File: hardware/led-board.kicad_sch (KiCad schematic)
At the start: 65 parts, among them J1 XT60PW-M, J2 PROG, J3 I2C, J4 CAN2, J5 XT30PW-F, J6 XT30PW-F, J7 MR30PW-FB, Q1 NCE0115K, Q2 NCE0115K, Q3 BSS138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

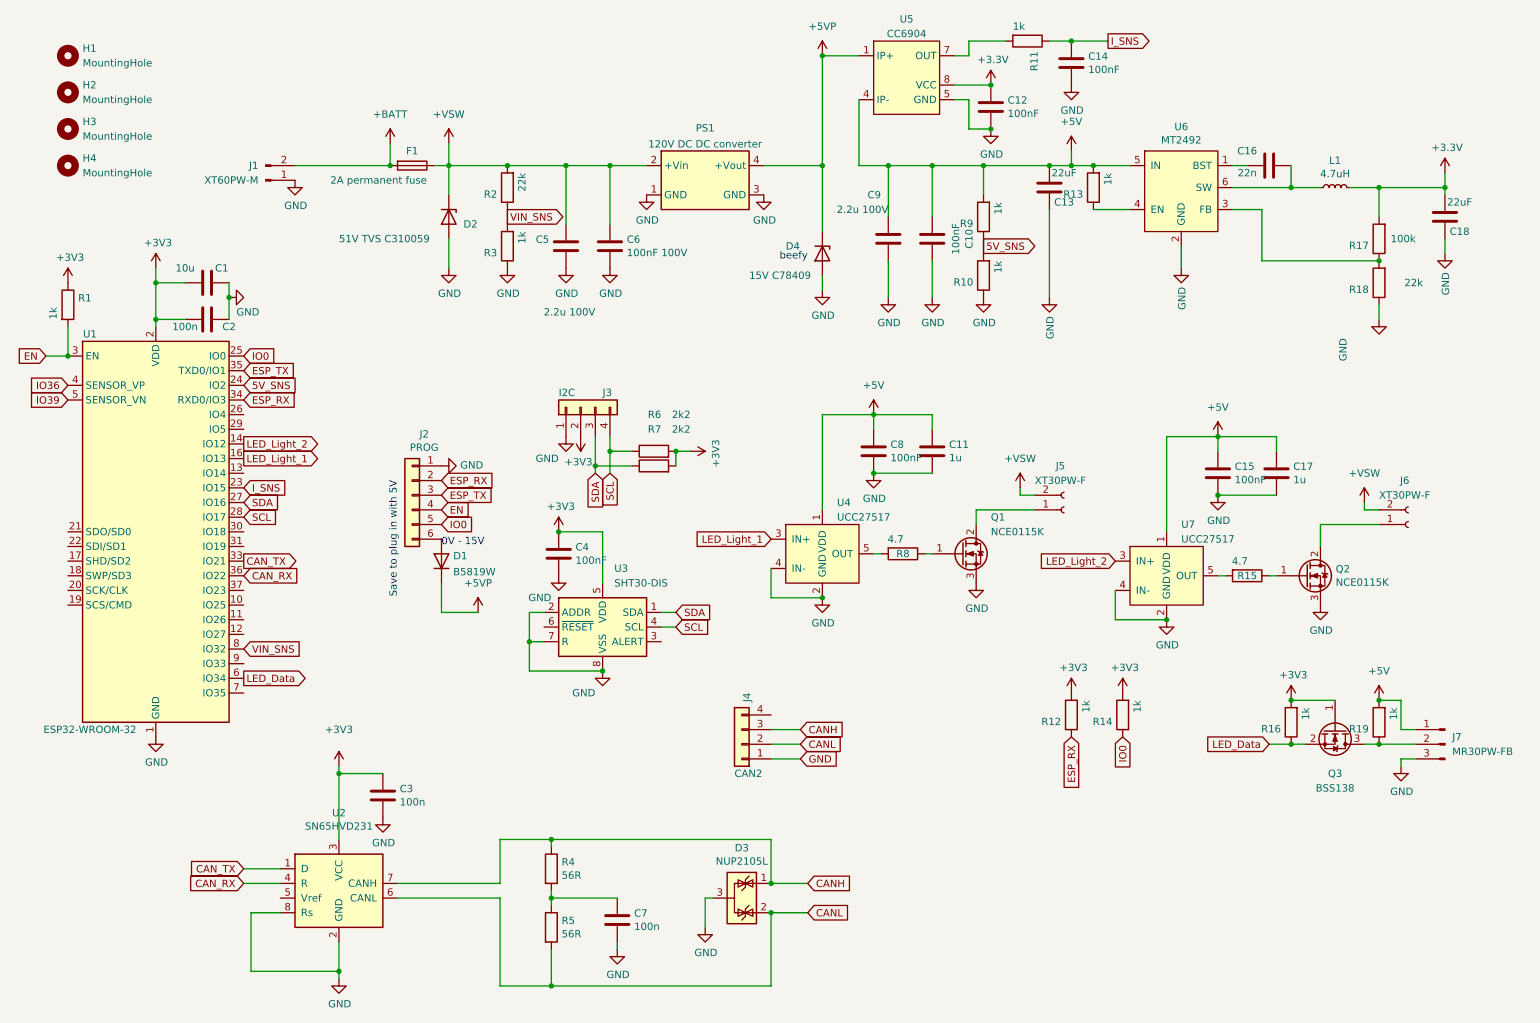
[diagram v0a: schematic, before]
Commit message: Updated wrong pins
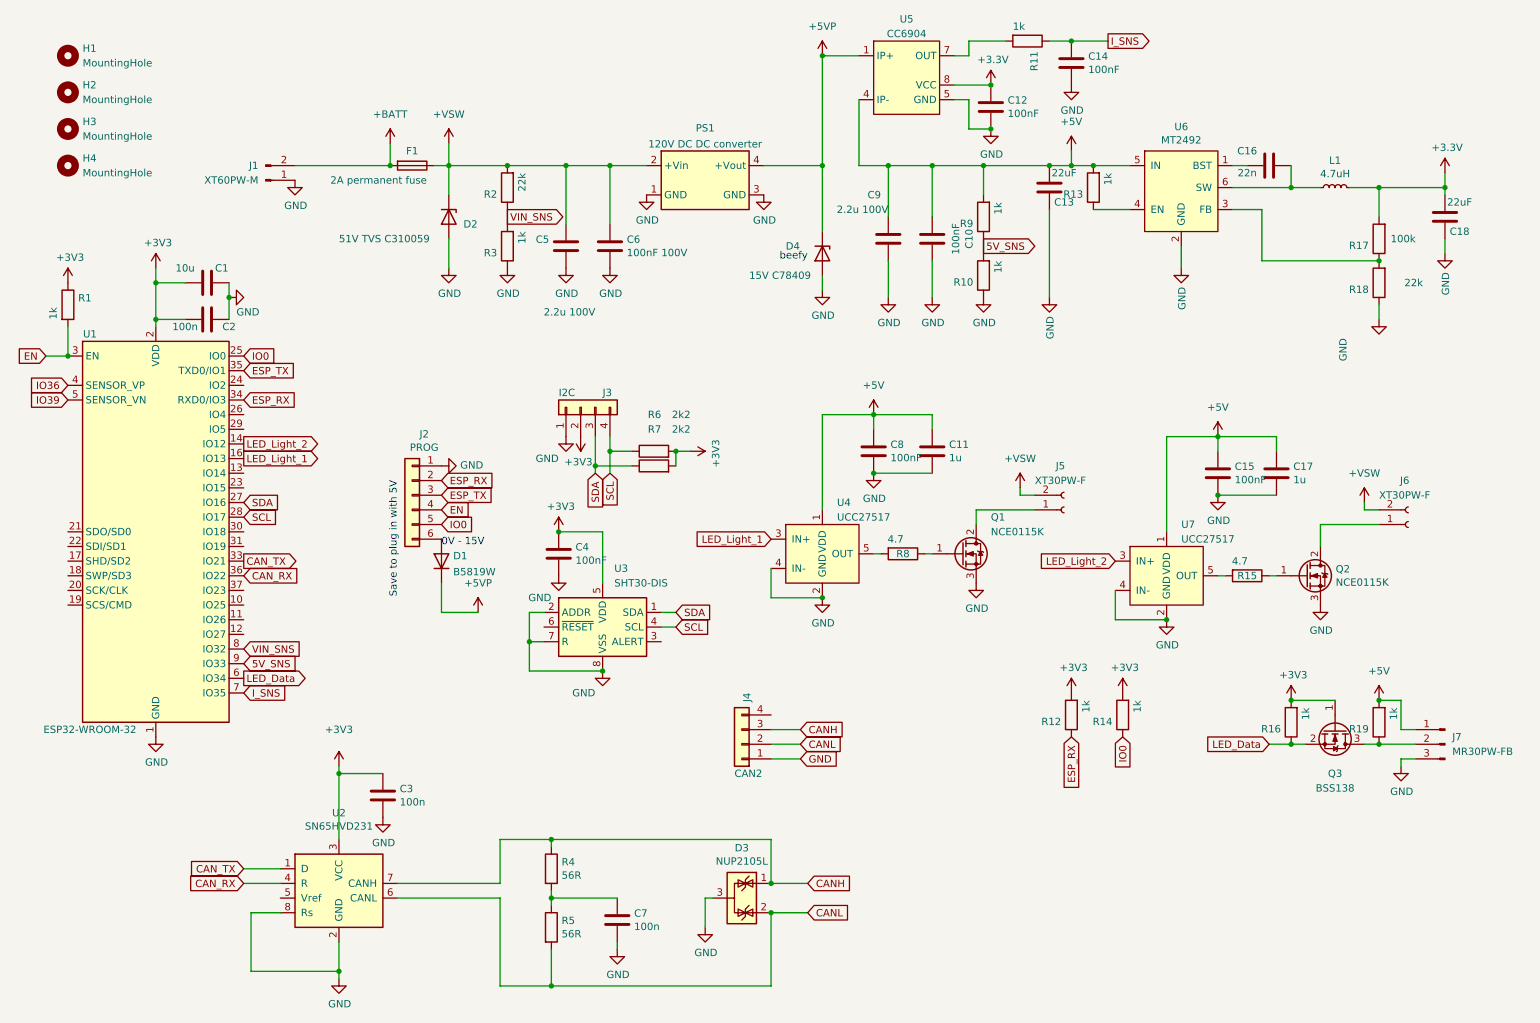
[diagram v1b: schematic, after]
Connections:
- net 5V_SNS: now also U1.9 (IO33); no longer U1.24 (IO2)
- net I_SNS: now also U1.7 (IO35); no longer U1.23 (IO15)
